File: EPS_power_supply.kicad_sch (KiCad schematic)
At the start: 6 parts

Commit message: Power supply
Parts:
- added D1, D2, D3, D4, D5, D6, D7: 1N4148WT, Diode_SMD:D_SOD-523, symbol Diode:1N4148WT
- added IC1: TPS7B8733QDDARQ1, PULSE_Library:DDA0008J-IPC_B, symbol PULSE_Library:TPS7B8733QDDARQ1
- added IC2: TPS7B8750QDDARQ1, PULSE_Library:DDA0008J-IPC_B, symbol PULSE_Library:TPS7B8750QDDARQ1
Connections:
- net GND: now also IC1.2 (NC_1), IC1.4 (NC_2), IC1.5 (GND), IC1.7 (NC_3), IC2.2 (NC_1), IC2.4 (NC_2), IC2.5 (GND), IC2.7 (NC_3)
- net VDDANA renamed 3V3
- net 3V3: now also D3.1 (K), D4.1 (K)
- new net: D5.1 (K), D7.2 (A)
- new net: D1.1 (K), IC2.8 (IN)
- new net: D2.1 (K), D3.2 (A)
- new net 3V3_LDO: D2.2 (A), IC1.1 (OUT)
- new net 3V3_PDU: D4.2 (A)
- new net 5V: D6.1 (K), D7.1 (K)
- new net 5V_LDO: D5.2 (A), IC1.8 (IN), IC2.1 (OUT)
- new net 5V_PDU: D6.2 (A)
- new net PV_in: D1.2 (A)
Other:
- moved on the sheet: C1, C2, C3, C4, C5, C6

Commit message: lastest
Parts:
- removed D3, D7: 1N4148WT, Diode_SMD:D_SOD-523, symbol Diode:1N4148WT
- added D24, D3: 1N5711, Diode_THT:D_DO-35_SOD27_P7.62mm_Horizontal, symbol Diode:1N5711
- added R_BYPASS1, R_BYPASS16: 0, Resistor_SMD:R_0603_1608Metric, symbol Device:R
- added TP1: 3V3_rail, TestPoint:TestPoint_Pad_D2.0mm, symbol Connector:TestPoint_Probe
- added TP2_3V_preOR1: ~, TestPoint:TestPoint_Pad_D2.0mm, symbol Connector:TestPoint_Probe
- added TP34: GND, TestPoint:TestPoint_Pad_D2.0mm, symbol Connector:TestPoint_Probe
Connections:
- net 3V3: now also D24.1 (K), R_BYPASS16.2, TP1.1
- net 3V3_LDO: now also TP2_3V_preOR1.1
- net 3V3_PDU: now also R_BYPASS16.1
- net 5V: now also D3.1 (K), R_BYPASS1.2
- net 5V_LDO: now also R_BYPASS1.1
- net GND: now also TP34.1
- net at D5.1 (K): now also D3.2 (A)
- net at D2.1 (K): now also D24.2 (A)
- no-connect marks 0 -> 4
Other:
- moved on the sheet: D5, D6

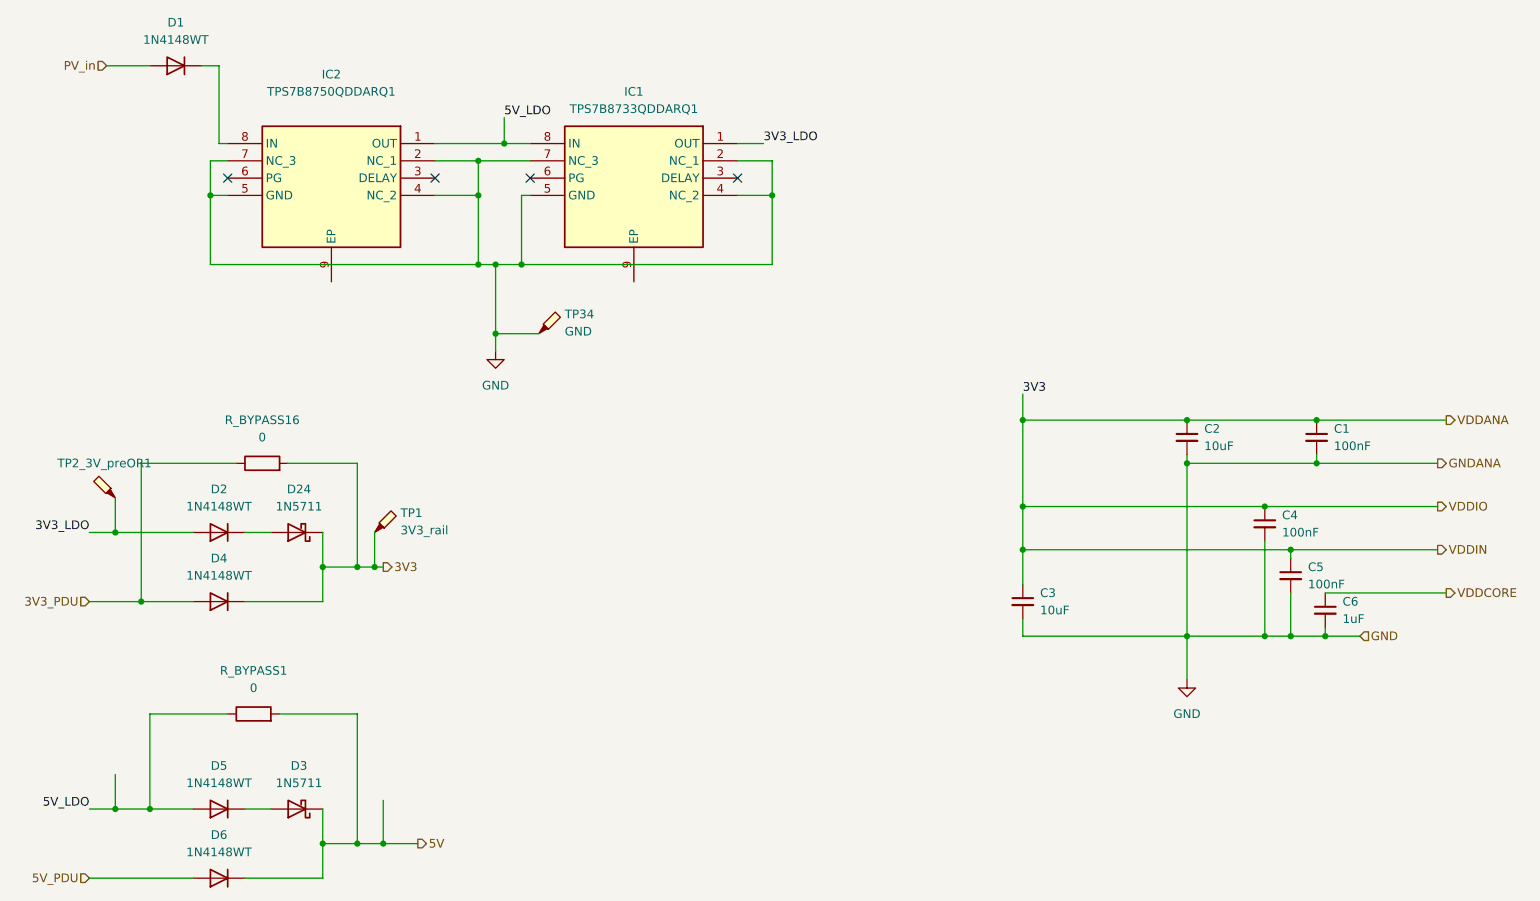
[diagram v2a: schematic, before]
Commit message: changed mcu power suppl
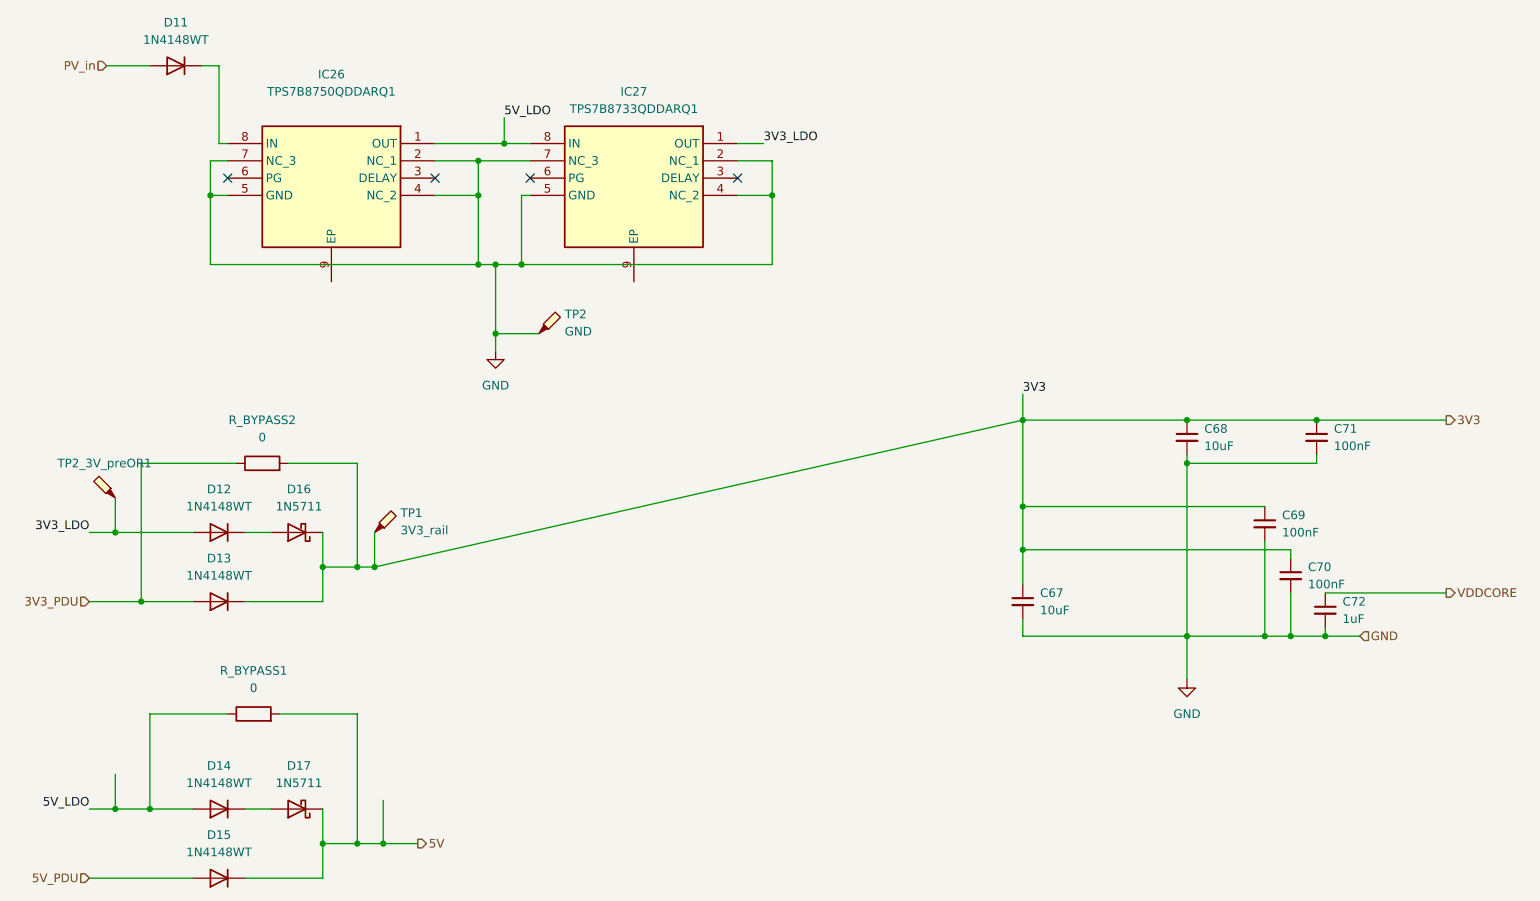
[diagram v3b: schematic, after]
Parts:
- renumbered C3 to C67, C2 to C68, C4 to C69, C5 to C70, C1 to C71, C6 to C72, D1 to D11, D2 to D12, D4 to D13, D5 to D14, D6 to D15, D24 to D16, D3 to D17, IC2 to IC26, IC1 to IC27, R_BYPASS16 to R_BYPASS2, TP34 to TP2
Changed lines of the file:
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@@
-	)
-	(junction
-		(at 210.82 100.33)
-		(diameter 0)
-		(color 0 0 0 0)
-	)
-	(junction
-		(at 218.44 93.98)
-		(diameter 0)
-		(color 0 0 0 0)
 	)
 	(junction
@@
 	)
 	(junction
-		(at 214.63 106.68)
-		(diameter 0)
-		(color 0 0 0 0)
-	)
-	(junction
 		(at 175.26 87.63)
 		(diameter 0)
@@
 	(wire
 		(pts
-			(xy 218.44 93.98) (xy 236.22 93.98)
-		)
-		(stroke
-			(width 0)
-			(type default)
-		)
-	)
-	(wire
-		(pts
-			(xy 214.63 106.68) (xy 236.22 106.68)
-		)
-		(stroke
-			(width 0)
-			(type default)
-		)
-	)
-	(wire
-		(pts
 			(xy 175.26 116.84) (xy 175.26 119.38)
 		)
@@
 	(wire
 		(pts
-			(xy 80.01 109.22) (xy 81.28 109.22)
-		)
-		(stroke
-			(width 0)
-			(type default)
-		)
-	)
-	(wire
-		(pts
 			(xy 45.72 114.3) (xy 53.34 114.3)
 		)
@@
 	(wire
 		(pts
+			(xy 80.01 109.22) (xy 175.26 87.63)
+		)
+		(stroke
+			(width 0)
+			(type default)
+		)
+	)
+	(wire
+		(pts
 			(xy 219.71 119.38) (xy 224.79 119.38)
 		)
@@
 		(pts
 			(xy 97.79 64.77) (xy 97.79 74.93)
-		)
-		(stroke
-			(width 0)
-			(type default)
-		)
-	)
-	(wire
-		(pts
-			(xy 210.82 100.33) (xy 236.22 100.33)
 		)
 		(stroke
@@
 		)
 	)
+	(label "3V3"
+		(at 175.26 83.82 0)
+		(effects
+			(font
+				(size 1.27 1.27)
+			)
+			(justify left bottom)
+		)
+	)
 	(label "3V3_LDO"
 		(at 38.1 104.14 180)
@@
 	(label "3V3_LDO"
 		(at 137.16 46.99 0)
-		(effects
-			(font
-				(size 1.27 1.27)
-			)
-			(justify left bottom)
-		)
-	)
-	(label "3V3"
-		(at 175.26 83.82 0)
 		(effects
 			(font
@@
 		)
 	)
-	(hierarchical_label "VDDIN"
-		(shape output)
-		(at 236.22 106.68 0)
-		(effects
-			(font
-				(size 1.27 1.27)
-			)
-			(justify left)
-		)
-	)
 	(hierarchical_label "3V3_PDU"
 		(shape input)
@@
 		)
 	)
-	(hierarchical_label "GNDANA"
-		(shape output)
-		(at 236.22 93.98 0)
-		(effects
-			(font
-				(size 1.27 1.27)
-			)
-			(justify left)
-		)
-	)
-	(hierarchical_label "VDDIO"
-		(shape output)
-		(at 236.22 100.33 0)
-		(effects
-			(font
-				(size 1.27 1.27)
-			)
-			(justify left)
-		)
-	)
 	(hierarchical_label "3V3"
-		(shape output)
-		(at 81.28 109.22 0)
-		(effects
-			(font
-				(size 1.27 1.27)
-			)
-			(justify left)
-		)
-	)
-	(hierarchical_label "VDDANA"
 		(shape output)
 		(at 237.49 87.63 0)
@@
 		(on_board yes)
 		(dnp no)
-		(property "Reference" "IC1"
+		(property "Reference" "IC27"
 			(at 118.11 39.37 0)
 			(effects
@@
 			(project ""
 				(path "/2de881bb-2e2a-47f9-96ed-b3393fa36b98/8bf4b950-7d1e-4a2d-ad03-078c0e232a33"
-					(reference "IC1")
+					(reference "IC27")
 					(unit 1)
 				)
@@
 		(dnp no)
 		(fields_autoplaced yes)
-		(property "Reference" "D5"
+		(property "Reference" "D14"
 			(at 57.15 138.43 0)
 			(effects
@@
 			(project "PULSE_ENG"
 				(path "/2de881bb-2e2a-47f9-96ed-b3393fa36b98/8bf4b950-7d1e-4a2d-ad03-078c0e232a33"
-					(reference "D5")
+					(reference "D14")
 					(unit 1)
 				)
@@
 		(dnp no)
 		(fields_autoplaced yes)
-		(property "Reference" "D4"
+		(property "Reference" "D13"
 			(at 57.15 107.95 0)
 			(effects
@@
 			(project "PULSE_ENG"
 				(path "/2de881bb-2e2a-47f9-96ed-b3393fa36b98/8bf4b950-7d1e-4a2d-ad03-078c0e232a33"
-					(reference "D4")
+					(reference "D13")
 					(unit 1)
 				)
@@
 		(dnp no)
 		(fields_autoplaced yes)
-		(property "Reference" "R_BYPASS16"
+		(property "Reference" "R_BYPASS2"
 			(at 63.5 87.63 90)
 			(effects
@@
 			(project "PULSE_ENG"
 				(path "/2de881bb-2e2a-47f9-96ed-b3393fa36b98/8bf4b950-7d1e-4a2d-ad03-078c0e232a33"
-					(reference "R_BYPASS16")
+					(reference "R_BYPASS2")
 					(unit 1)
 				)
@@
 		(dnp no)
 		(fields_autoplaced yes)
-		(property "Reference" "C2"
+		(property "Reference" "C68"
 			(at 201.93 88.9062 0)
 			(effects
@@
 			(project "PULSE_ENG"
 				(path "/2de881bb-2e2a-47f9-96ed-b3393fa36b98/8bf4b950-7d1e-4a2d-ad03-078c0e232a33"
-					(reference "C2")
+					(reference "C68")
 					(unit 1)
 				)
@@
 		(dnp no)
 		(fields_autoplaced yes)
-		(property "Reference" "#PWR03"
+		(property "Reference" "#PWR047"
 			(at 199.39 132.08 0)
 			(effects
@@
 			(project "PULSE_ENG"
 				(path "/2de881bb-2e2a-47f9-96ed-b3393fa36b98/8bf4b950-7d1e-4a2d-ad03-078c0e232a33"
-					(reference "#PWR03")
+					(reference "#PWR047")
 					(unit 1)
 				)
@@
 		(dnp no)
 		(fields_autoplaced yes)
-		(property "Reference" "D24"
+		(property "Reference" "D16"
 			(at 68.8975 97.79 0)
 			(effects
@@
 			(project ""
 				(path "/2de881bb-2e2a-47f9-96ed-b3393fa36b98/8bf4b950-7d1e-4a2d-ad03-078c0e232a33"
-					(reference "D24")
+					(reference "D16")
 					(unit 1)
 				)
@@
 		(dnp no)
 		(fields_autoplaced yes)
-		(property "Reference" "C4"
+		(property "Reference" "C69"
 			(at 213.36 101.6062 0)
 			(effects
@@
 			(project "PULSE_ENG"
 				(path "/2de881bb-2e2a-47f9-96ed-b3393fa36b98/8bf4b950-7d1e-4a2d-ad03-078c0e232a33"
-					(reference "C4")
+					(reference "C69")
 					(unit 1)
 				)
@@
 		(dnp no)
 		(fields_autoplaced yes)
-		(property "Reference" "D6"
+		(property "Reference" "D15"
 			(at 57.15 148.59 0)
 			(effects
@@
 			(project "PULSE_ENG"
 				(path "/2de881bb-2e2a-47f9-96ed-b3393fa36b98/8bf4b950-7d1e-4a2d-ad03-078c0e232a33"
-					(reference "D6")
+					(reference "D15")
 					(unit 1)
 				)
@@
 		(dnp no)
 		(fields_autoplaced yes)
-		(property "Reference" "D1"
+		(property "Reference" "D11"
 			(at 50.8 29.21 0)
 			(effects
@@
 			(project ""
 				(path "/2de881bb-2e2a-47f9-96ed-b3393fa36b98/8bf4b950-7d1e-4a2d-ad03-078c0e232a33"
-					(reference "D1")
+					(reference "D11")
 					(unit 1)
 				)
@@
 		(dnp no)
 		(fields_autoplaced yes)
-		(property "Reference" "C1"
+		(property "Reference" "C71"
 			(at 220.98 88.9062 0)
 			(effects
@@
 			(project "PULSE_ENG"
 				(path "/2de881bb-2e2a-47f9-96ed-b3393fa36b98/8bf4b950-7d1e-4a2d-ad03-078c0e232a33"
-					(reference "C1")
+					(reference "C71")
 					(unit 1)
 				)
@@
 		(dnp no)
 		(fields_autoplaced yes)
-		(property "Reference" "D2"
+		(property "Reference" "D12"
 			(at 57.15 97.79 0)
 			(effects
@@
 			(project "PULSE_ENG"
 				(path "/2de881bb-2e2a-47f9-96ed-b3393fa36b98/8bf4b950-7d1e-4a2d-ad03-078c0e232a33"
-					(reference "D2")
+					(reference "D12")
 					(unit 1)
 				)
@@
 		(dnp no)
 		(fields_autoplaced yes)
-		(property "Reference" "#PWR01"
+		(property "Reference" "#PWR046"
 			(at 97.79 83.82 0)
 			(effects
@@
 			(project ""
 				(path "/2de881bb-2e2a-47f9-96ed-b3393fa36b98/8bf4b950-7d1e-4a2d-ad03-078c0e232a33"
-					(reference "#PWR01")
+					(reference "#PWR046")
 					(unit 1)
 				)
@@
 		(dnp no)
 		(fields_autoplaced yes)
-		(property "Reference" "TP34"
+		(property "Reference" "TP2"
 			(at 107.95 72.0724 0)
 			(effects
@@
 			(project ""
 				(path "/2de881bb-2e2a-47f9-96ed-b3393fa36b98/8bf4b950-7d1e-4a2d-ad03-078c0e232a33"
-					(reference "TP34")
+					(reference "TP2")
 					(unit 1)
 				)
@@
 		(dnp no)
 		(fields_autoplaced yes)
-		(property "Reference" "D3"
+		(property "Reference" "D17"
 			(at 68.8975 138.43 0)
 			(effects
@@
 			(project "PULSE_ENG"
 				(path "/2de881bb-2e2a-47f9-96ed-b3393fa36b98/8bf4b950-7d1e-4a2d-ad03-078c0e232a33"
-					(reference "D3")
+					(reference "D17")
 					(unit 1)
 				)
@@
 		(on_board yes)
 		(dnp no)
-		(property "Reference" "IC2"
+		(property "Reference" "IC26"
 			(at 73.66 36.83 0)
 			(effects
@@
 			(project ""
 				(path "/2de881bb-2e2a-47f9-96ed-b3393fa36b98/8bf4b950-7d1e-4a2d-ad03-078c0e232a33"
-					(reference "IC2")
+					(reference "IC26")
 					(unit 1)
 				)
@@
 		(dnp no)
 		(fields_autoplaced yes)
-		(property "Reference" "C5"
+		(property "Reference" "C70"
 			(at 217.17 109.2262 0)
 			(effects
@@
 			(project "PULSE_ENG"
 				(path "/2de881bb-2e2a-47f9-96ed-b3393fa36b98/8bf4b950-7d1e-4a2d-ad03-078c0e232a33"
-					(reference "C5")
+					(reference "C70")
 					(unit 1)
 				)
@@
 		(dnp no)
 		(fields_autoplaced yes)
-		(property "Reference" "C6"
+		(property "Reference" "C72"
 			(at 222.25 114.3062 0)
 			(effects
@@
 			(project "PULSE_ENG"
 				(path "/2de881bb-2e2a-47f9-96ed-b3393fa36b98/8bf4b950-7d1e-4a2d-ad03-078c0e232a33"
-					(reference "C6")
+					(reference "C72")
 					(unit 1)
 				)
@@
 		(dnp no)
 		(fields_autoplaced yes)
-		(property "Reference" "C3"
+		(property "Reference" "C67"
 			(at 177.8 113.0362 0)
 			(effects
@@
 			(project "PULSE_ENG"
 				(path "/2de881bb-2e2a-47f9-96ed-b3393fa36b98/8bf4b950-7d1e-4a2d-ad03-078c0e232a33"
-					(reference "C3")
+					(reference "C67")
 					(unit 1)
 				)
